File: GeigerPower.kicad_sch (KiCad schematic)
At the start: 40 parts, among them J1 ConnPulse, Q1 MMBTA42, Q2 BC817, U1 40106

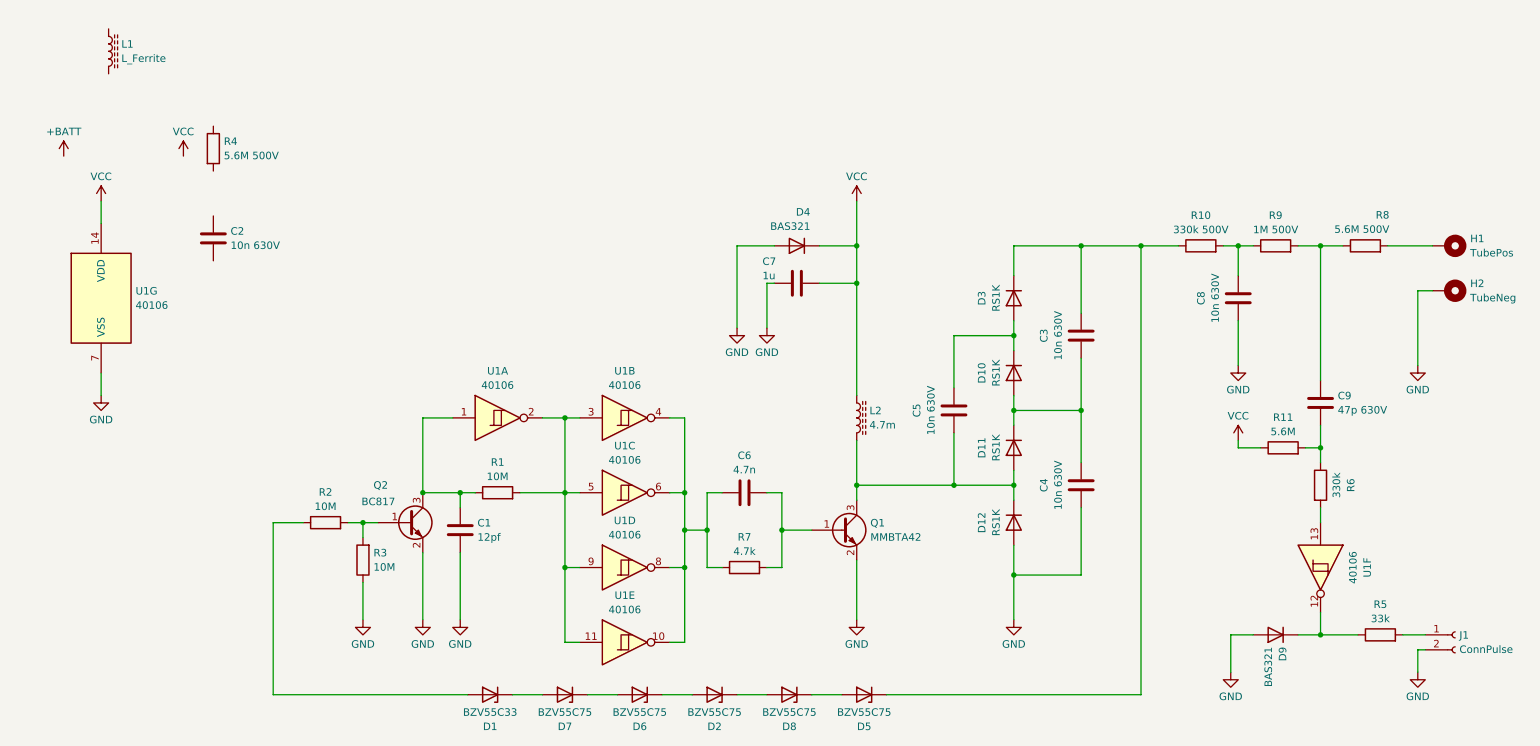
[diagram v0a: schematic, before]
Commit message: Input power finished
Added battery connector, input RC-filter.
Rewired protection diode from generator to filter output.
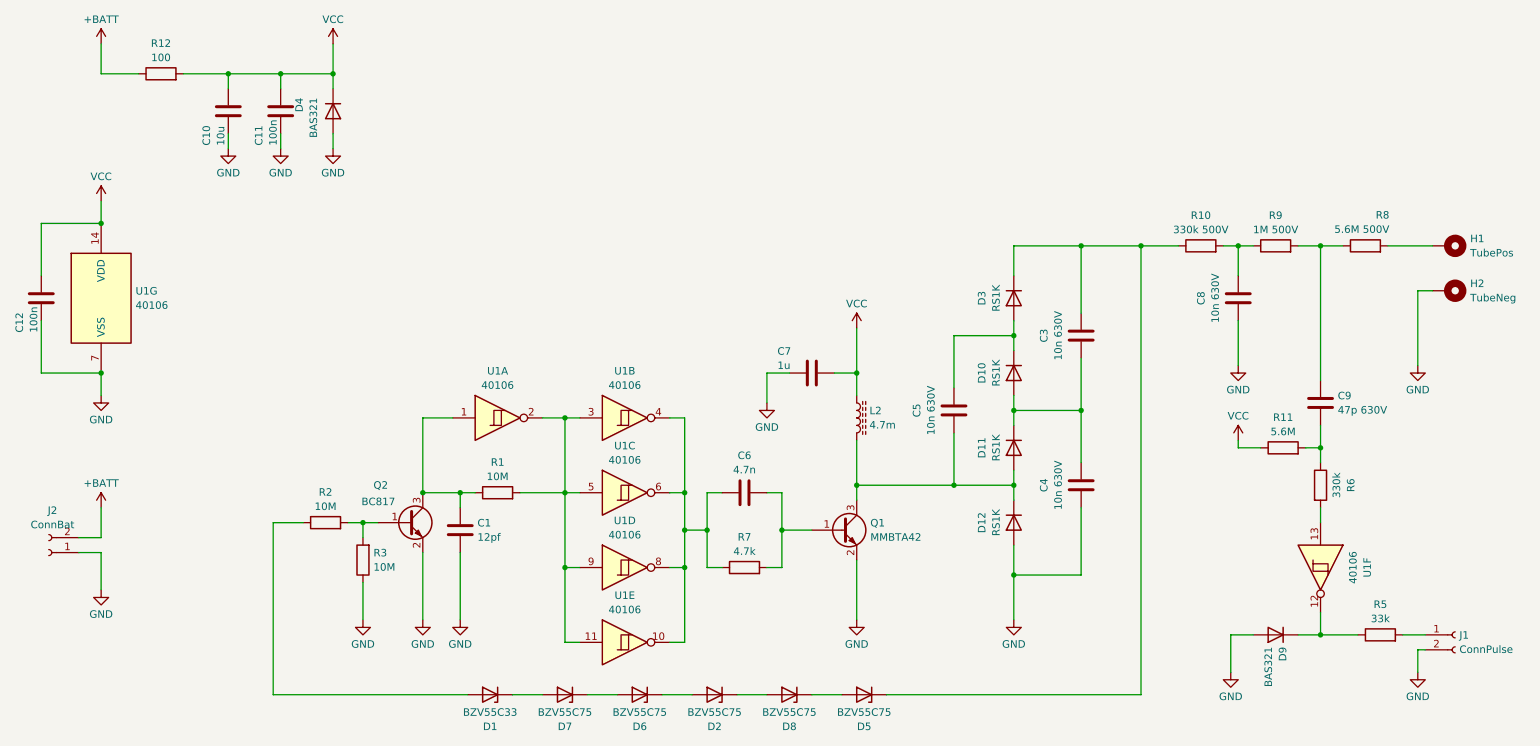
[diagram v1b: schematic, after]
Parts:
- removed C2: 10n 630V, Capacitor_SMD:C_1206_3216Metric_Pad1.33x1.80mm_HandSolder, symbol Device:C
- removed L1: L_Ferrite, symbol Device:L_Ferrite
- removed R4: 5.6M 500V, Resistor_SMD:R_2512_6332Metric_Pad1.40x3.35mm_HandSolder, symbol Device:R
- added C10: 10u, Capacitor_SMD:C_0805_2012Metric_Pad1.18x1.45mm_HandSolder, symbol Device:C
- added C11, C12: 100n, Capacitor_SMD:C_0805_2012Metric_Pad1.18x1.45mm_HandSolder, symbol Device:C
- added J2: ConnBat, symbol Connector:Conn_01x02_Socket
- added R12: 100, Resistor_SMD:R_0805_2012Metric_Pad1.20x1.40mm_HandSolder, symbol Device:R
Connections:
- net +BATT: now also J2.2 (Pin_2), R12.1
- net GND: now also C10.2, C11.2, C12.2, J2.1 (Pin_1)
- net VCC: now also C10.1, C11.1, C12.1, R12.2
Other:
- moved on the sheet: C7, D4

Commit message: Finished schematics
Applied some fixes. Assigned symbols.
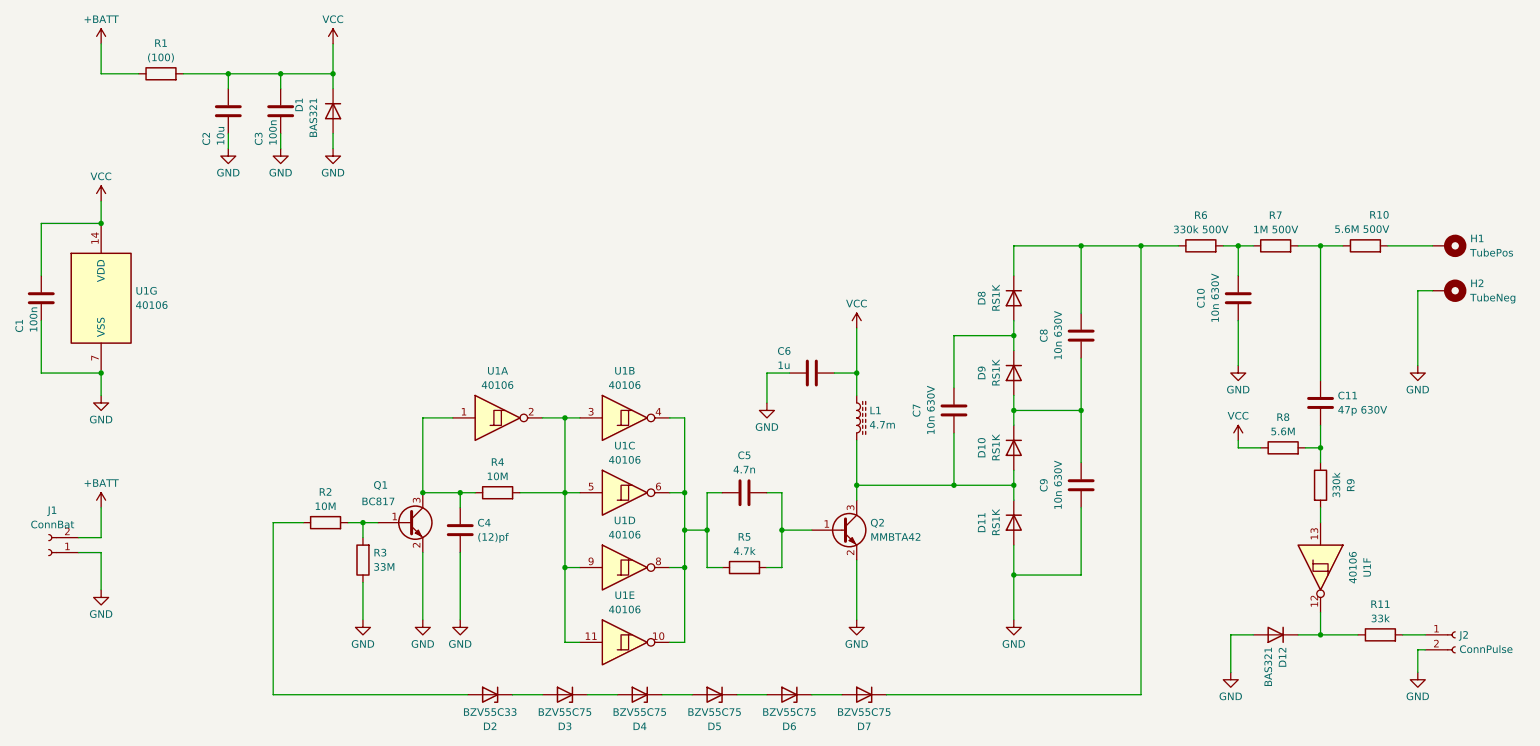
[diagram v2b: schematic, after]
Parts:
- C4: renamed from C1; value 12pf -> (12)pf
- H1, H2: footprint (none) -> MountingHole:MountingHole_2.7mm_M2.5_DIN965_Pad
- J1: renamed from J2; footprint (none) -> Connector_JST:JST_XH_S2B-XH-A-1_1x02_P2.50mm_Horizontal
- J2: renamed from J1; footprint (none) -> Connector_JST:JST_XH_S2B-XH-A-1_1x02_P2.50mm_Horizontal
- R1: renamed from R12; value 100 -> (100)
- R3: value 10M -> 33M
- U1: footprint (none) -> Package_SO:SOIC-14_3.9x8.7mm_P1.27mm
- renumbered C12 to C1, C8 to C10, C9 to C11, C10 to C2, C11 to C3, C6 to C5, C7 to C6, C5 to C7, C3 to C8, C4 to C9, D4 to D1, D11 to D10, D12 to D11, D9 to D12, D1 to D2, D7 to D3, D6 to D4, D2 to D5, D8 to D6, D5 to D7, D3 to D8, D10 to D9, L2 to L1, Q2 to Q1, Q1 to Q2, R8 to R10, R5 to R11, R1 to R4, R7 to R5, R10 to R6, R9 to R7, R11 to R8, R6 to R9

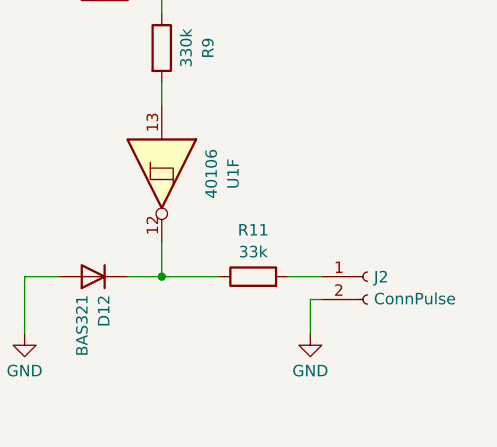
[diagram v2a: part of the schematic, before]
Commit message: Connectors rewired
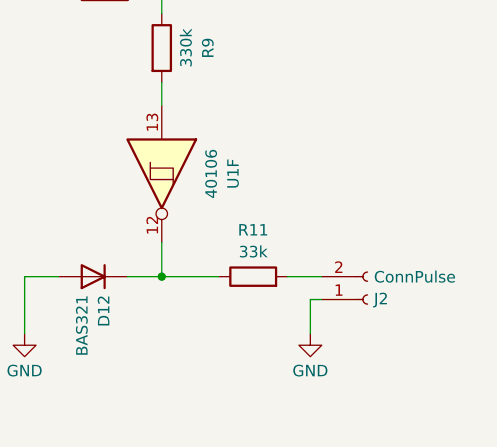
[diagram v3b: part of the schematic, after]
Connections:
- net GND: now also J2.1 (Pin_1); no longer J2.2 (Pin_2)
- net at R11.2: now also J2.2 (Pin_2); no longer J2.1 (Pin_1)
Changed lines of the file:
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@@
 	(wire
 		(pts
+			(xy 25.4 105.41) (xy 29.21 105.41)
+		)
+		(stroke
+			(width 0)
+			(type default)
+		)
+	)
+	(wire
+		(pts
 			(xy 83.82 105.41) (xy 83.82 116.84)
 		)
@@
 	(wire
 		(pts
-			(xy 25.4 105.41) (xy 29.21 105.41)
-		)
-		(stroke
-			(width 0)
-			(type default)
-		)
-	)
-	(wire
-		(pts
 			(xy 233.68 87.63) (xy 236.22 87.63)
 		)
@@
 		(on_board yes)
 		(dnp no)
-		(fields_autoplaced yes)
 		(property "Reference" "J1"
 			(at 20.955 98.2683 0)
@@
 	(symbol
 		(lib_id "Connector:Conn_01x02_Socket")
-		(at 259.08 119.38 0)
+		(at 259.08 121.92 0)
+		(mirror x)
 		(unit 1)
 		(exclude_from_sim no)
@@
 		(on_board yes)
 		(dnp no)
-		(fields_autoplaced yes)
 		(property "Reference" "J2"
-			(at 259.7912 119.4378 0)
+			(at 259.7912 121.8622 0)
 			(effects
 				(font
@@
 		)
 		(property "Value" "ConnPulse"
-			(at 259.7912 121.8621 0)
+			(at 259.7912 119.4379 0)
 			(effects
 				(font
@@
 		)
 		(property "Footprint" "Connector_JST:JST_XH_S2B-XH-A-1_1x02_P2.50mm_Horizontal"
-			(at 259.08 119.38 0)
+			(at 259.08 121.92 0)
 			(effects
 				(font
@@
 		)
 		(property "Datasheet" "~"
-			(at 259.08 119.38 0)
+			(at 259.08 121.92 0)
 			(effects
 				(font
@@
 		)
 		(property "Description" "Generic connector, single row, 01x02, script generated"
-			(at 259.08 119.38 0)
+			(at 259.08 121.92 0)
 			(effects
 				(font

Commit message: Adjustments, HV-rules
Added high coltage rules. Small silkscreen fixes applied. Another contour edit performed.
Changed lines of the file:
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@@
 		)
 	)
+	(netclass_flag ""
+		(length 2.54)
+		(shape round)
+		(at 236.22 53.34 0)
+		(fields_autoplaced yes)
+		(effects
+			(font
+				(size 1.27 1.27)
+			)
+			(justify left bottom)
+		)
+		(property "Netclass" "High Voltage"
+			(at 236.9185 50.8 0)
+			(effects
+				(font
+					(size 1.27 1.27)
+					(italic yes)
+				)
+				(justify left)
+			)
+		)
+	)
+	(netclass_flag ""
+		(length 2.54)
+		(shape round)
+		(at 250.19 53.34 0)
+		(fields_autoplaced yes)
+		(effects
+			(font
+				(size 1.27 1.27)
+			)
+			(justify left bottom)
+		)
+		(property "Netclass" "High Voltage"
+			(at 250.8885 50.8 0)
+			(effects
+				(font
+					(size 1.27 1.27)
+					(italic yes)
+				)
+				(justify left)
+			)
+		)
+	)
+	(netclass_flag ""
+		(length 2.54)
+		(shape round)
+		(at 222.25 53.34 0)
+		(fields_autoplaced yes)
+		(effects
+			(font
+				(size 1.27 1.27)
+			)
+			(justify left bottom)
+		)
+		(property "Netclass" "High Voltage"
+			(at 222.9485 50.8 0)
+			(effects
+				(font
+					(size 1.27 1.27)
+					(italic yes)
+				)
+				(justify left)
+			)
+		)
+	)
+	(netclass_flag ""
+		(length 2.54)
+		(shape round)
+		(at 195.58 53.34 0)
+		(fields_autoplaced yes)
+		(effects
+			(font
+				(size 1.27 1.27)
+			)
+			(justify left bottom)
+		)
+		(property "Netclass" "High Voltage"
+			(at 196.2785 50.8 0)
+			(effects
+				(font
+					(size 1.27 1.27)
+					(italic yes)
+				)
+				(justify left)
+			)
+		)
+	)
 	(symbol
 		(lib_id "power:GND")
@@
 		(on_board yes)
 		(dnp no)
-		(fields_autoplaced yes)
 		(property "Reference" "R7"
-			(at 228.6 48.1795 90)
+			(at 228.6 57.0117 90)
 			(effects
 				(font
@@
 		)
 		(property "Value" "1M 500V"
-			(at 228.6 50.6038 90)
+			(at 228.6 59.436 90)
 			(effects
 				(font
@@
 		(dnp no)
 		(property "Reference" "R10"
-			(at 247.904 48.1217 90)
+			(at 247.396 57.2657 90)
 			(effects
 				(font
@@
 		)
 		(property "Value" "5.6M 500V"
-			(at 247.904 50.546 90)
+			(at 247.396 59.69 90)
 			(effects
 				(font
